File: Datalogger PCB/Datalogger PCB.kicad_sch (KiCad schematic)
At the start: 20 parts, among them J1 Conn_01x02_Pin, U2 W25Q128JVS

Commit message: Turn Schematic into PCB
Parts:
- D2: footprint (none) -> Breakout Boards:RGB_LED
- R1, R10, R2, R4, R5, R6, R7, R8, R9: footprint Resistor_THT:R_Axial_DIN0207_L6.3mm_D2.5mm_P2.54mm_Vertical -> Resistor_THT:R_Axial_DIN0207_L6.3mm_D2.5mm_P7.62mm_Horizontal
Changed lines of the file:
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@@
       (effects (font (size 1.27 1.27)))
     )
-    (property "Footprint" "Resistor_THT:R_Axial_DIN0207_L6.3mm_D2.5mm_P2.54mm_Vertical" (at 164.338 120.015 90)
+    (property "Footprint" "Resistor_THT:R_Axial_DIN0207_L6.3mm_D2.5mm_P7.62mm_Horizontal" (at 164.338 120.015 90)
       (effects (font (size 1.27 1.27)) hide)
     )
@@
       (effects (font (size 1.27 1.27)))
     )
-    (property "Footprint" "Resistor_THT:R_Axial_DIN0207_L6.3mm_D2.5mm_P2.54mm_Vertical" (at 219.71 28.067 90)
+    (property "Footprint" "Resistor_THT:R_Axial_DIN0207_L6.3mm_D2.5mm_P7.62mm_Horizontal" (at 219.71 28.067 90)
       (effects (font (size 1.27 1.27)) hide)
     )
@@
       (effects (font (size 1.27 1.27)))
     )
-    (property "Footprint" "Resistor_THT:R_Axial_DIN0207_L6.3mm_D2.5mm_P2.54mm_Vertical" (at 48.895 74.803 90)
+    (property "Footprint" "Resistor_THT:R_Axial_DIN0207_L6.3mm_D2.5mm_P7.62mm_Horizontal" (at 48.895 74.803 90)
       (effects (font (size 1.27 1.27)) hide)
     )
@@
       (effects (font (size 1.27 1.27)))
     )
-    (property "Footprint" "" (at 40.005 74.295 0)
+    (property "Footprint" "Breakout Boards:RGB_LED" (at 40.005 74.295 0)
       (effects (font (size 1.27 1.27)) hide)
     )
@@
       (effects (font (size 1.27 1.27)))
     )
-    (property "Footprint" "Resistor_THT:R_Axial_DIN0207_L6.3mm_D2.5mm_P2.54mm_Vertical" (at 219.71 49.022 90)
+    (property "Footprint" "Resistor_THT:R_Axial_DIN0207_L6.3mm_D2.5mm_P7.62mm_Horizontal" (at 219.71 49.022 90)
       (effects (font (size 1.27 1.27)) hide)
     )
@@
       (effects (font (size 1.27 1.27)))
     )
-    (property "Footprint" "Resistor_THT:R_Axial_DIN0207_L6.3mm_D2.5mm_P2.54mm_Vertical" (at 163.322 120.015 90)
+    (property "Footprint" "Resistor_THT:R_Axial_DIN0207_L6.3mm_D2.5mm_P7.62mm_Horizontal" (at 163.322 120.015 90)
       (effects (font (size 1.27 1.27)) hide)
     )
@@
       (effects (font (size 1.27 1.27)))
     )
-    (property "Footprint" "Resistor_THT:R_Axial_DIN0207_L6.3mm_D2.5mm_P2.54mm_Vertical" (at 220.345 69.342 90)
+    (property "Footprint" "Resistor_THT:R_Axial_DIN0207_L6.3mm_D2.5mm_P7.62mm_Horizontal" (at 220.345 69.342 90)
       (effects (font (size 1.27 1.27)) hide)
     )
@@
       (effects (font (size 1.27 1.27)))
     )
-    (property "Footprint" "Resistor_THT:R_Axial_DIN0207_L6.3mm_D2.5mm_P2.54mm_Vertical" (at 127 96.393 90)
+    (property "Footprint" "Resistor_THT:R_Axial_DIN0207_L6.3mm_D2.5mm_P7.62mm_Horizontal" (at 127 96.393 90)
       (effects (font (size 1.27 1.27)) hide)
     )
@@
       (effects (font (size 1.27 1.27)))
     )
-    (property "Footprint" "Resistor_THT:R_Axial_DIN0207_L6.3mm_D2.5mm_P2.54mm_Vertical" (at 48.895 69.723 90)
+    (property "Footprint" "Resistor_THT:R_Axial_DIN0207_L6.3mm_D2.5mm_P7.62mm_Horizontal" (at 48.895 69.723 90)
       (effects (font (size 1.27 1.27)) hide)
     )
@@
       (effects (font (size 1.27 1.27)))
     )
-    (property "Footprint" "Resistor_THT:R_Axial_DIN0207_L6.3mm_D2.5mm_P2.54mm_Vertical" (at 48.895 79.883 90)
-      (effects (font (size 1.27 1.27)) hide)
-    )
+    (property "Footprint" "Resistor_THT:R_Axial_DIN0207_L6.3mm_D2.5mm_P7.62mm_Horizontal" (at 48.895 79.883 90)
+      (effects (font (size 1.27 1.27)) hide)
+    )

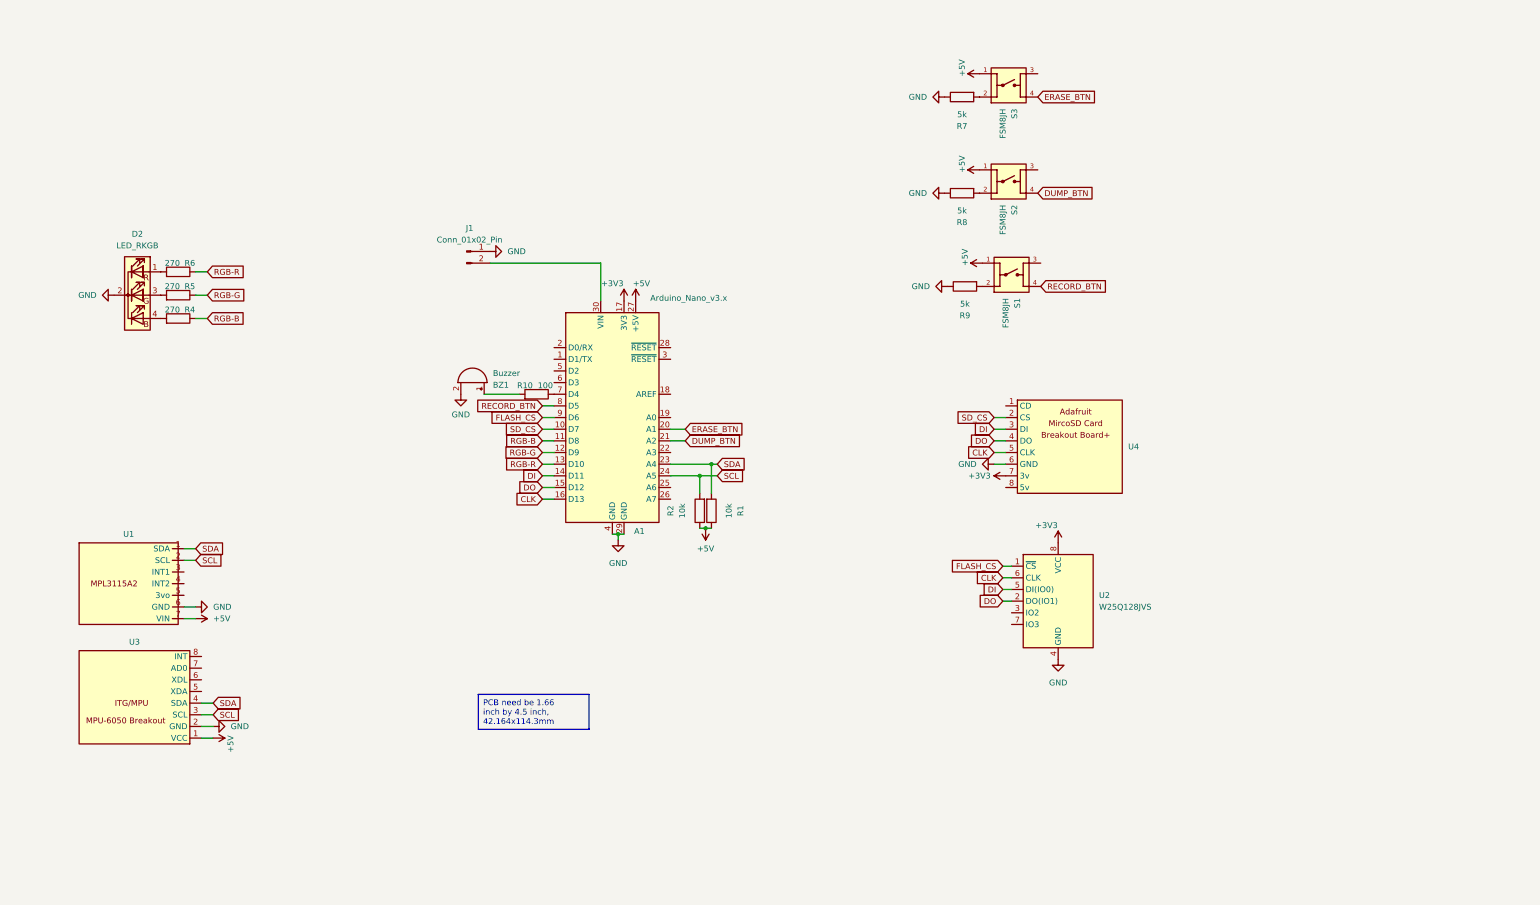
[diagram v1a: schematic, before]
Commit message: Teensy 4.1 based datalogger with SMD parts
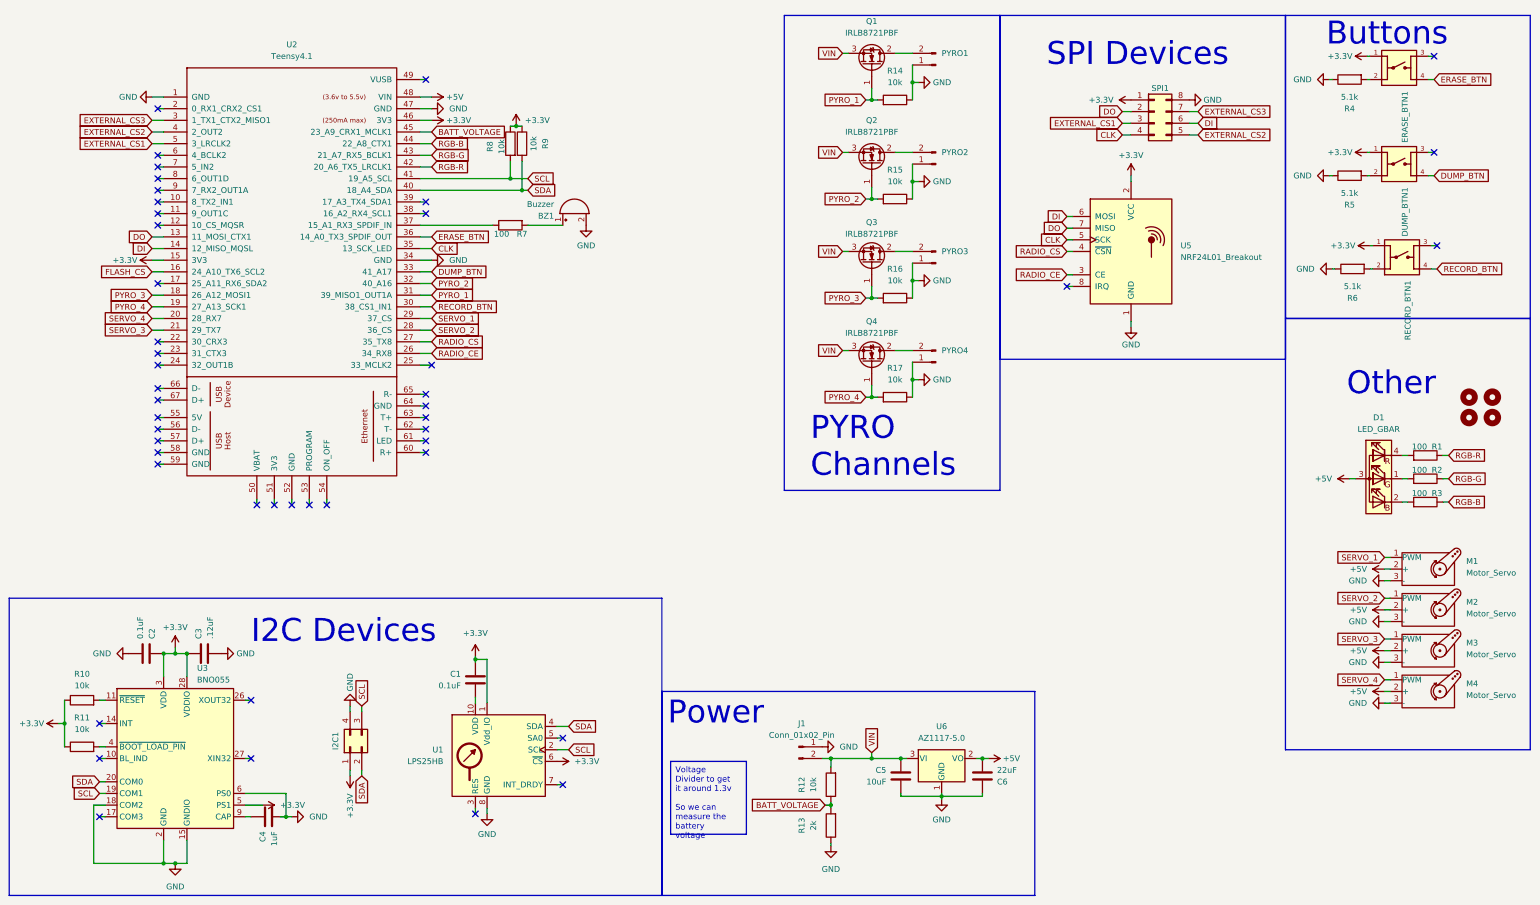
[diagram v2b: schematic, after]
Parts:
- removed A1: Arduino_Nano_v3.x, Module:Arduino_Nano, symbol MCU_Module:Arduino_Nano_v3.x
- removed D2: LED_RKGB, Breakout Boards:RGB_LED, symbol Device:LED_RKGB
- removed S1, S2, S3: FSM8JH, Push Button:SW_FSM8JH, symbol Push Button:FSM8JH
- removed U1: ~, Breakout Boards:MPL3115A2, symbol My Parts:MPL3115A2
- removed U2: W25Q128JVS, Package_SO:SOIC-8_5.23x5.23mm_P1.27mm, symbol Memory_Flash:W25Q128JVS
- removed U3: ~, Datalogging Breakout:MPU-6050 Breakout, symbol Datalogging Breakout Board:MPU-6050
- removed U4: ~, Breakout Boards:Adafruit Micro-SD Breakout Board+, symbol Datalogging Breakout Board:Adafruit_MicroSD_Card_Breakout_Board
- added C1, C2: 0.1uF, Resistor_SMD:R_0603_1608Metric_Pad0.98x0.95mm_HandSolder, symbol Device:C
- added C3: .12uF, Resistor_SMD:R_0603_1608Metric_Pad0.98x0.95mm_HandSolder, symbol Device:C
- added C4: 1uF, Resistor_SMD:R_0603_1608Metric_Pad0.98x0.95mm_HandSolder, symbol Device:C
- added C5: 10uF, Resistor_SMD:R_0603_1608Metric_Pad0.98x0.95mm_HandSolder, symbol Device:C
- added C6: 22uF, Resistor_SMD:R_0603_1608Metric_Pad0.98x0.95mm_HandSolder, symbol Device:C
- added D1: LED_GBAR, Led:LED_GBAR, symbol Device:LED_GBAR
- added DUMP_BTN1, ERASE_BTN1, RECORD_BTN1: FSM8JH, Push Button:SW_FSM8JH, symbol Push Button:FSM8JH
- added H1, H2, H3, H4: MountingHole, MountingHole:MountingHole_2.2mm_M2, symbol Mechanical:MountingHole
- added I2C1: Conn_02x02_Counter_Clockwise, Connector_PinHeader_1.27mm:PinHeader_2x02_P1.27mm_Vertical, symbol Connector_Generic:Conn_02x02_Counter_Clockwise
- added M1, M2, M3, M4: Motor_Servo, Connector_PinHeader_2.54mm:PinHeader_1x03_P2.54mm_Vertical, symbol Motor:Motor_Servo
- added PYRO1, PYRO2, PYRO3, PYRO4: Conn_01x02_Pin, Connector_PinHeader_1.27mm:PinHeader_1x02_P1.27mm_Vertical, symbol Connector:Conn_01x02_Pin
- added Q1, Q2, Q3, Q4: IRLB8721PBF, Package_TO_SOT_THT:TO-220-3_Vertical, symbol Transistor_FET:IRLB8721PBF
- added R11, R12, R14, R15, R16, R17: 10k, Resistor_SMD:R_0603_1608Metric_Pad0.98x0.95mm_HandSolder, symbol Device:R
- added R13: 2k, Resistor_SMD:R_0603_1608Metric_Pad0.98x0.95mm_HandSolder, symbol Device:R
- added R3: 100, Resistor_SMD:R_0603_1608Metric_Pad0.98x0.95mm_HandSolder, symbol Device:R
- added SPI1: Conn_02x04_Counter_Clockwise, Connector_PinHeader_1.27mm:PinHeader_2x04_P1.27mm_Vertical, symbol Connector_Generic:Conn_02x04_Counter_Clockwise
- added U1: LPS25HB, Package_LGA:ST_HLGA-10_2.5x2.5mm_P0.6mm_LayoutBorder3x2y, symbol Sensor_Pressure:LPS25HB
- added U2: Teensy4.1, Teensy4.1:Teensy41, symbol Teensy4.1:Teensy4.1
- added U3: BNO055, Package_LGA:LGA-28_5.2x3.8mm_P0.5mm, symbol Sensor_Motion:BNO055
- added U5: NRF24L01_Breakout, RF_Module:nRF24L01_Breakout, symbol RF:NRF24L01_Breakout
- added U6: AZ1117-5.0, Package_TO_SOT_SMD:SOT-223, symbol Regulator_Linear:AZ1117-5.0
- J1: now left out of the parts list
- R1, R2: value 10k -> 100; footprint Resistor_THT:R_Axial_DIN0207_L6.3mm_D2.5mm_P7.62mm_Horizontal -> Resistor_SMD:R_0603_1608Metric_Pad0.98x0.95mm_HandSolder
- R10: value 100 -> 10k; footprint Resistor_THT:R_Axial_DIN0207_L6.3mm_D2.5mm_P7.62mm_Horizontal -> Resistor_SMD:R_0603_1608Metric_Pad0.98x0.95mm_HandSolder
- R4, R5, R6: value 270 -> 5.1k; footprint Resistor_THT:R_Axial_DIN0207_L6.3mm_D2.5mm_P7.62mm_Horizontal -> Resistor_SMD:R_0603_1608Metric_Pad0.98x0.95mm_HandSolder
- R7: value 5k -> 100; footprint Resistor_THT:R_Axial_DIN0207_L6.3mm_D2.5mm_P7.62mm_Horizontal -> Resistor_SMD:R_0603_1608Metric_Pad0.98x0.95mm_HandSolder
- R8, R9: value 5k -> 10k; footprint Resistor_THT:R_Axial_DIN0207_L6.3mm_D2.5mm_P7.62mm_Horizontal -> Resistor_SMD:R_0603_1608Metric_Pad0.98x0.95mm_HandSolder
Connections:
- net +5V: now also C6.2, D1.3 (A), M1.2 (+), M2.2 (+), M3.2 (+), M4.2 (+), U2.48 (VIN), U6.2 (VO); no longer R1.1, R2.1
- net CLK: now also SPI1.4 (Pin_4), U2.35 (13_SCK_LED), U5.5 (SCK)
- net DI: now also SPI1.6 (Pin_6), U2.14 (12_MISO_MQSL), U5.6 (MOSI)
- net DO: now also SPI1.2 (Pin_2), U2.13 (11_MOSI_CTX1), U5.7 (MISO)
- net DUMP_BTN: now also DUMP_BTN1.4, U2.33 (41_A17)
- net ERASE_BTN: now also ERASE_BTN1.4, U2.36 (14_A0_TX3_SPDIF_OUT)
- net FLASH_CS: now also U2.16 (24_A10_TX6_SCL2)
- net GND: now also R4.1, R5.1, R6.1, C2.2, C3.2, C4.2, C5.2, C6.1, I2C1.4 (Pin_4), M1.3 (-), M2.3 (-), M3.3 (-), M4.3 (-), PYRO1.1 (Pin_1), PYRO2.1 (Pin_1), PYRO3.1 (Pin_1), PYRO4.1 (Pin_1), R13.1, R14.1, R15.1, R16.1, R17.1, SPI1.8 (Pin_8), U1.8 (GND), U1.9 (GND), U2.1 (GND), U2.34 (GND), U2.47 (GND), U3.15 (GNDIO), U3.16 (GNDIO), U3.18 (COM2), U3.2 (GND), U3.25 (GNDIO), U3.6 (PS0), U5.1 (GND), U6.1 (GND); no longer R7.1, R8.1, R9.1
- net RECORD_BTN: now also RECORD_BTN1.4, U2.30 (38_CS1_IN1)
- net RGB-B: now also R3.1, U2.44 (22_A8_CTX1); no longer R4.1
- net RGB-G: now also R2.1, U2.43 (21_A7_RX5_BCLK1); no longer R5.1
- net RGB-R: now also R1.1, U2.42 (20_A6_TX5_LRCLK1); no longer R6.1
- net SCL: now also R8.2, I2C1.3 (Pin_3), U1.2 (SCL), U2.41 (19_A5_SCL), U3.19 (COM1); no longer R2.2
- net SDA: now also R9.2, I2C1.2 (Pin_2), U1.4 (SDA), U2.40 (18_A4_SDA), U3.20 (COM0); no longer R1.2
- net at R7.2: now also BZ1.1 (-)
- net VIN: now reaches J1.2 (Pin_2)
- net VIN: now also C5.1, Q1.3 (S), Q2.3 (S), Q3.3 (S), Q4.3 (S), R12.2, U6.3 (VI)
- net at R5.2: now also DUMP_BTN1.2
- net at R10.2: now also U3.11 (~{RESET}); no longer BZ1.1 (-)
- net +3.3V: now reaches R10.1
- net +3.3V: now also R8.1, R9.1, C1.1, C2.1, C3.1, DUMP_BTN1.1, ERASE_BTN1.1, I2C1.1 (Pin_1), R11.1, RECORD_BTN1.1, SPI1.1 (Pin_1), U1.1 (Vdd_IO), U1.6 (~{CS}), U2.15 (3V3), U2.46 (3V3), U3.28 (VDDIO), U3.3 (VDD), U3.5 (PS1), U5.2 (VCC)
- net at R6.2: now also RECORD_BTN1.2
- net at R4.2: now also ERASE_BTN1.2
- new net: PYRO2.2 (Pin_2), Q2.2 (D)
- new net: R11.2, U3.4 (~{BOOT_LOAD_PIN})
- new net: D1.1 (GK), R2.2
- new net: PYRO4.2 (Pin_2), Q4.2 (D)
- new net: PYRO1.2 (Pin_2), Q1.2 (D)
- new net: D1.2 (BK), R3.2
- new net: D1.4 (RK), R1.2
- new net: C1.2, U1.10 (VDD)
- new net: PYRO3.2 (Pin_2), Q3.2 (D)
- new net: C4.1, U3.9 (CAP)
- new net: R7.1, U2.37 (15_A1_RX3_SPDIF_IN)
- new net BATT_VOLTAGE: R12.1, R13.2, U2.45 (23_A9_CRX1_MCLK1)
- new net EXTERNAL_CS1: SPI1.3 (Pin_3), U2.5 (3_LRCLK2)
- new net EXTERNAL_CS2: SPI1.5 (Pin_5), U2.4 (2_OUT2)
- new net EXTERNAL_CS3: SPI1.7 (Pin_7), U2.3 (1_TX1_CTX2_MISO1)
- new net PYRO_1: Q1.1 (G), R14.2, U2.31 (39_MISO1_OUT1A)
- new net PYRO_2: Q2.1 (G), R15.2, U2.32 (40_A16)
- new net PYRO_3: Q3.1 (G), R16.2, U2.18 (26_A12_MOSI1)
- new net PYRO_4: Q4.1 (G), R17.2, U2.19 (27_A13_SCK1)
- new net RADIO_CE: U2.26 (34_RX8), U5.3 (CE)
- new net RADIO_CS: U2.27 (35_TX8), U5.4 (~{CSN})
- new net SERVO_1: M1.1 (PWM), U2.29 (37_CS)
- new net SERVO_2: M2.1 (PWM), U2.28 (36_CS)
- new net SERVO_3: M3.1 (PWM), U2.21 (29_TX7)
- new net SERVO_4: M4.1 (PWM), U2.20 (28_RX7)
- no-connect marks 0 -> 46
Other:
- note added: "Buttons"
- note added: "I2C Devices"
- note added: "Other"
- note added: "PYRO Channels"
- note added: "Power"
- note added: "SPI Devices"

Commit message: Rev2 done?
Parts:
- renumbered Q4 to Q3, Q3 to Q4, R17 to R16, R16 to R17
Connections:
- net FLASH_CS: no longer names the net of U2.16 (24_A10_TX6_SCL2)
- no-connect marks 46 -> 47
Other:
- moved on the sheet: PYRO1, PYRO2, PYRO3, PYRO4, R14, R15, R16, R17, U5

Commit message: V2 of the PCB
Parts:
- removed ERASE_BTN1: FSM8JH, Push Button:SW_FSM8JH, symbol Push Button:FSM8JH
- removed PYRO1, PYRO2, PYRO3, PYRO4: Conn_01x02_Pin, Connector_PinHeader_1.27mm:PinHeader_1x02_P1.27mm_Vertical, symbol Connector:Conn_01x02_Pin
- removed Q1, Q2, Q3, Q4: IRLB8721PBF, Package_TO_SOT_THT:TO-220-3_Vertical, symbol Transistor_FET:IRLB8721PBF
- removed R14, R15, R16, R17: 10k, Resistor_SMD:R_0603_1608Metric_Pad0.98x0.95mm_HandSolder, symbol Device:R
- removed R4: 5.1k, Resistor_SMD:R_0603_1608Metric_Pad0.98x0.95mm_HandSolder, symbol Device:R
- removed U6: AZ1117-5.0, Package_TO_SOT_SMD:SOT-223, symbol Regulator_Linear:AZ1117-5.0
- added PYRO_1-2, PYRO_3-4: Screw_Terminal_01x04, TerminalBlock:TerminalBlock_bornier-4_P5.08mm, symbol Connector:Screw_Terminal_01x04
- added U4: AMS1117-5.0, Package_TO_SOT_SMD:SOT-223-3_TabPin2, symbol Regulator_Linear:AMS1117-5.0
- added U6, U7, U8, U9: VN5E160STR-E, SOIC127P600X175-8N:SOIC127P600X175-8N, symbol VN5E160STR-E:VN5E160STR-E
- renumbered U2 to U1, U3 to U2, U1 to U3
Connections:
- net +5V: now also U4.2 (VO)
- net BATT_VOLTAGE: now also R13.1; no longer R13.2
- net ERASE_BTN: now also U1.38 (16_A2_RX4_SCL1); no longer U1.36 (14_A0_TX3_SPDIF_OUT)
- net GND: now also R13.2, PYRO_1-2.2 (Pin_2), PYRO_1-2.4 (Pin_4), PYRO_3-4.2 (Pin_2), PYRO_3-4.4 (Pin_4), U4.1 (GND), U6.1 (GND), U7.1 (GND), U8.1 (GND), U9.1 (GND); no longer R13.1
- net PYRO_1: now also U6.2 (INPUT)
- net PYRO_2: now also U1.36 (14_A0_TX3_SPDIF_OUT), U7.2 (INPUT); no longer U1.32 (40_A16)
- net PYRO_3: now also U1.19 (27_A13_SCK1), U8.2 (INPUT); no longer U1.18 (26_A12_MOSI1)
- net PYRO_4: now also U1.17 (25_A11_RX6_SDA2), U9.2 (INPUT); no longer U1.19 (27_A13_SCK1)
- net SERVO_3: now also U1.20 (28_RX7); no longer U1.21 (29_TX7)
- net SERVO_4: now also U1.21 (29_TX7); no longer U1.20 (28_RX7)
- net VIN: now also U4.3 (VI), U6.5 (VCC), U6.8 (VCC), U7.5 (VCC), U7.8 (VCC), U8.5 (VCC), U8.8 (VCC), U9.5 (VCC), U9.8 (VCC)
- net PYRO_4_STATUS: now reaches U1.16 (24_A10_TX6_SCL2)
- net PYRO_4_STATUS: now also U9.3 (STATUS)
- net at R7.1: now also U1.39 (17_A3_TX4_SDA1); no longer U1.37 (15_A1_RX3_SPDIF_IN)
- new net: PYRO_3-4.1 (Pin_1), U8.6 (OUTPUT), U8.7 (OUTPUT)
- new net: PYRO_3-4.3 (Pin_3), U9.6 (OUTPUT), U9.7 (OUTPUT)
- new net: PYRO_1-2.3 (Pin_3), U7.6 (OUTPUT), U7.7 (OUTPUT)
- new net: PYRO_1-2.1 (Pin_1), U6.6 (OUTPUT), U6.7 (OUTPUT)
- new net PYRO_1_STATUS: U1.32 (40_A16), U6.3 (STATUS)
- new net PYRO_2_STATUS: U1.37 (15_A1_RX3_SPDIF_IN), U7.3 (STATUS)
- new net PYRO_3_STATUS: U1.18 (26_A12_MOSI1), U8.3 (STATUS)
- no-connect marks 47 -> 46
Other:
- note added: "Teensy 4.1"
- note removed: "PYRO Channels"
- moved on the sheet: BZ1, C5, C6, DUMP_BTN1, J1, R12, R13, R5, R6, R7, R8, R9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

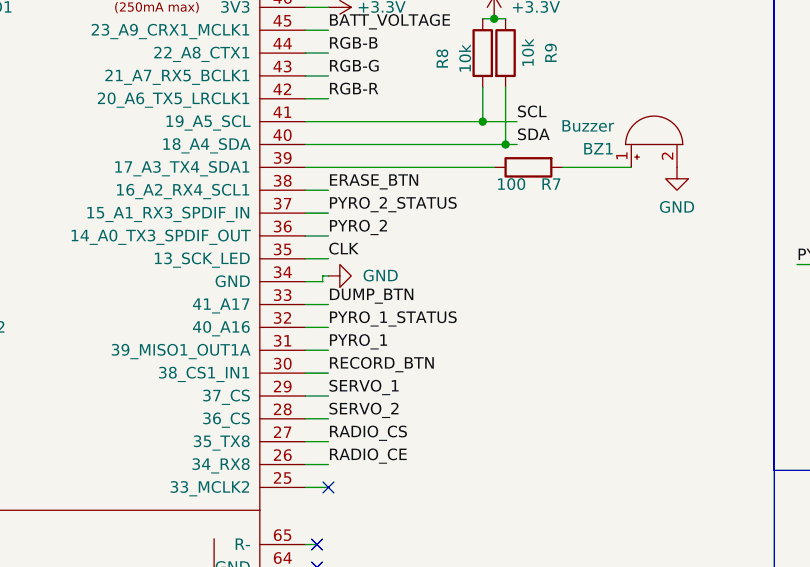
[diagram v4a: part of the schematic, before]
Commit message: Coverted to 2 layer board
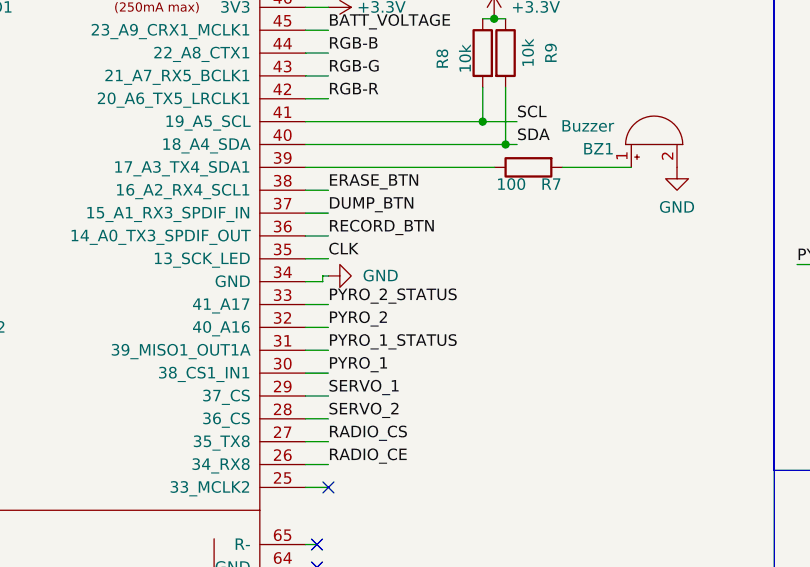
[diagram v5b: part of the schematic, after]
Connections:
- net DUMP_BTN: now also U1.37 (15_A1_RX3_SPDIF_IN); no longer U1.33 (41_A17)
- net PYRO_1: now also U1.30 (38_CS1_IN1); no longer U1.31 (39_MISO1_OUT1A)
- net PYRO_1_STATUS: now also U1.31 (39_MISO1_OUT1A); no longer U1.32 (40_A16)
- net PYRO_2: now also U1.32 (40_A16); no longer U1.36 (14_A0_TX3_SPDIF_OUT)
- net PYRO_2_STATUS: now also U1.33 (41_A17); no longer U1.37 (15_A1_RX3_SPDIF_IN)
- net RECORD_BTN: now also U1.36 (14_A0_TX3_SPDIF_OUT); no longer U1.30 (38_CS1_IN1)
